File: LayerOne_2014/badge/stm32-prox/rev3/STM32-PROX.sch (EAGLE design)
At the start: 271 parts, among them IC1 IC_TPS6120XQFN10, IC10 74XX244, IC105 MCP1824T-250, IC106 MCP1824T-120, IC11 CD4066, IC13 PQ1X331M2ZP-3V3-LDO-SOT-23-5, IC14 AD8052, IC2 STM32F1_HIGH_DENSITY_LQFP64LQ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, IC3 PQ1X331M2ZP-3V3-LDO-SOT-23-5, IC4 HCU-INVERTER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

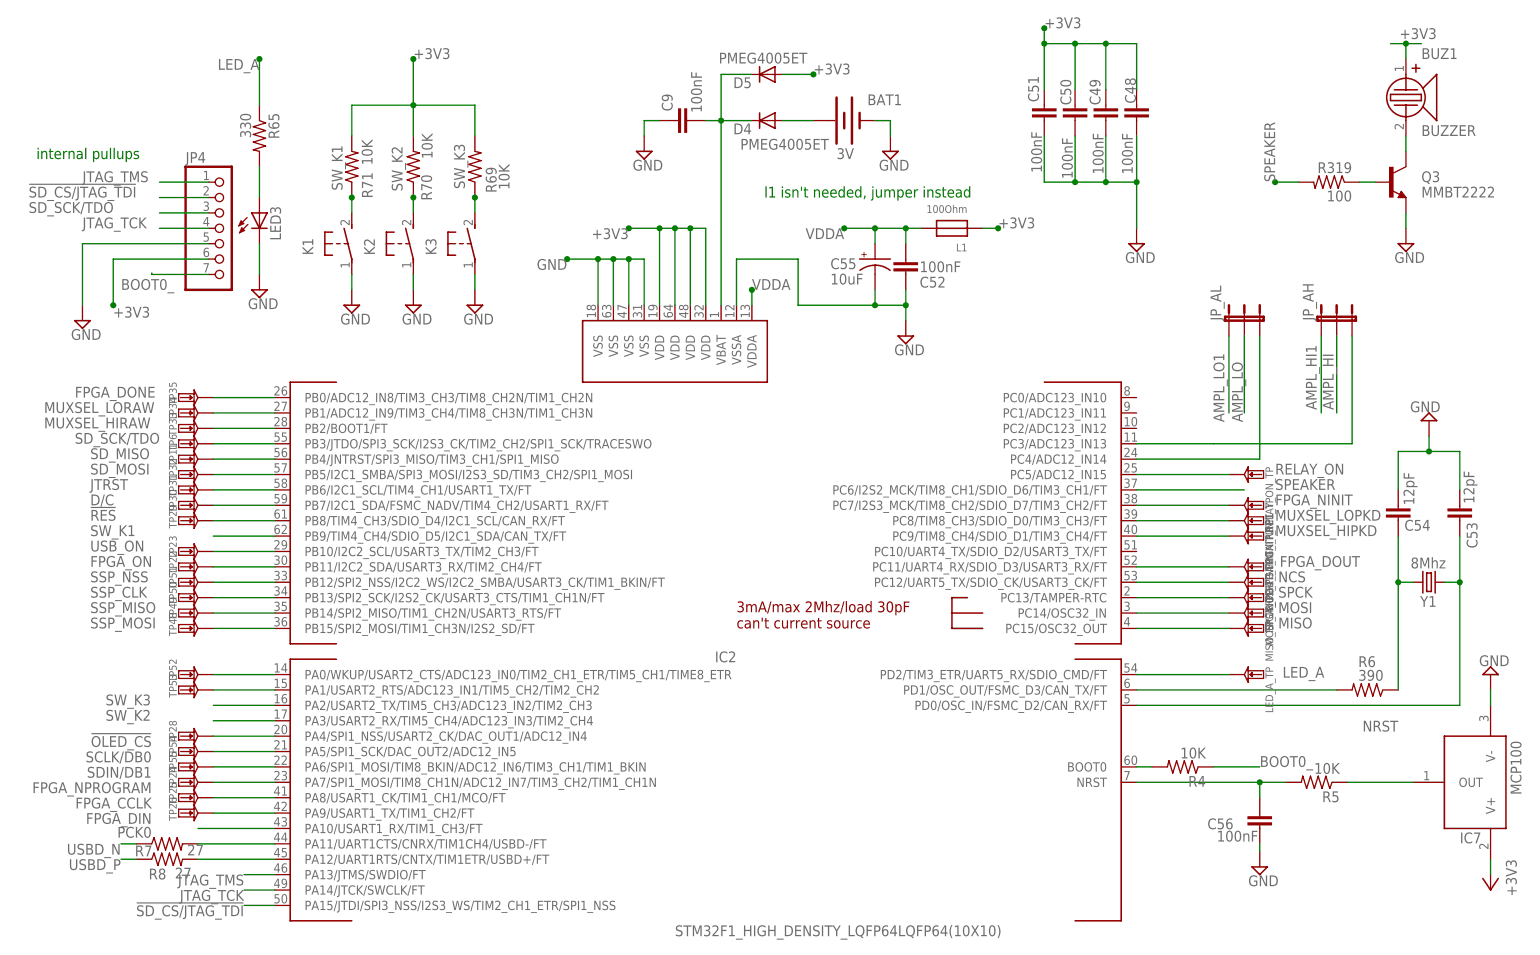
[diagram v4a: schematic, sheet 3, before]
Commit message: PB6 fixed on schematic for stm32f
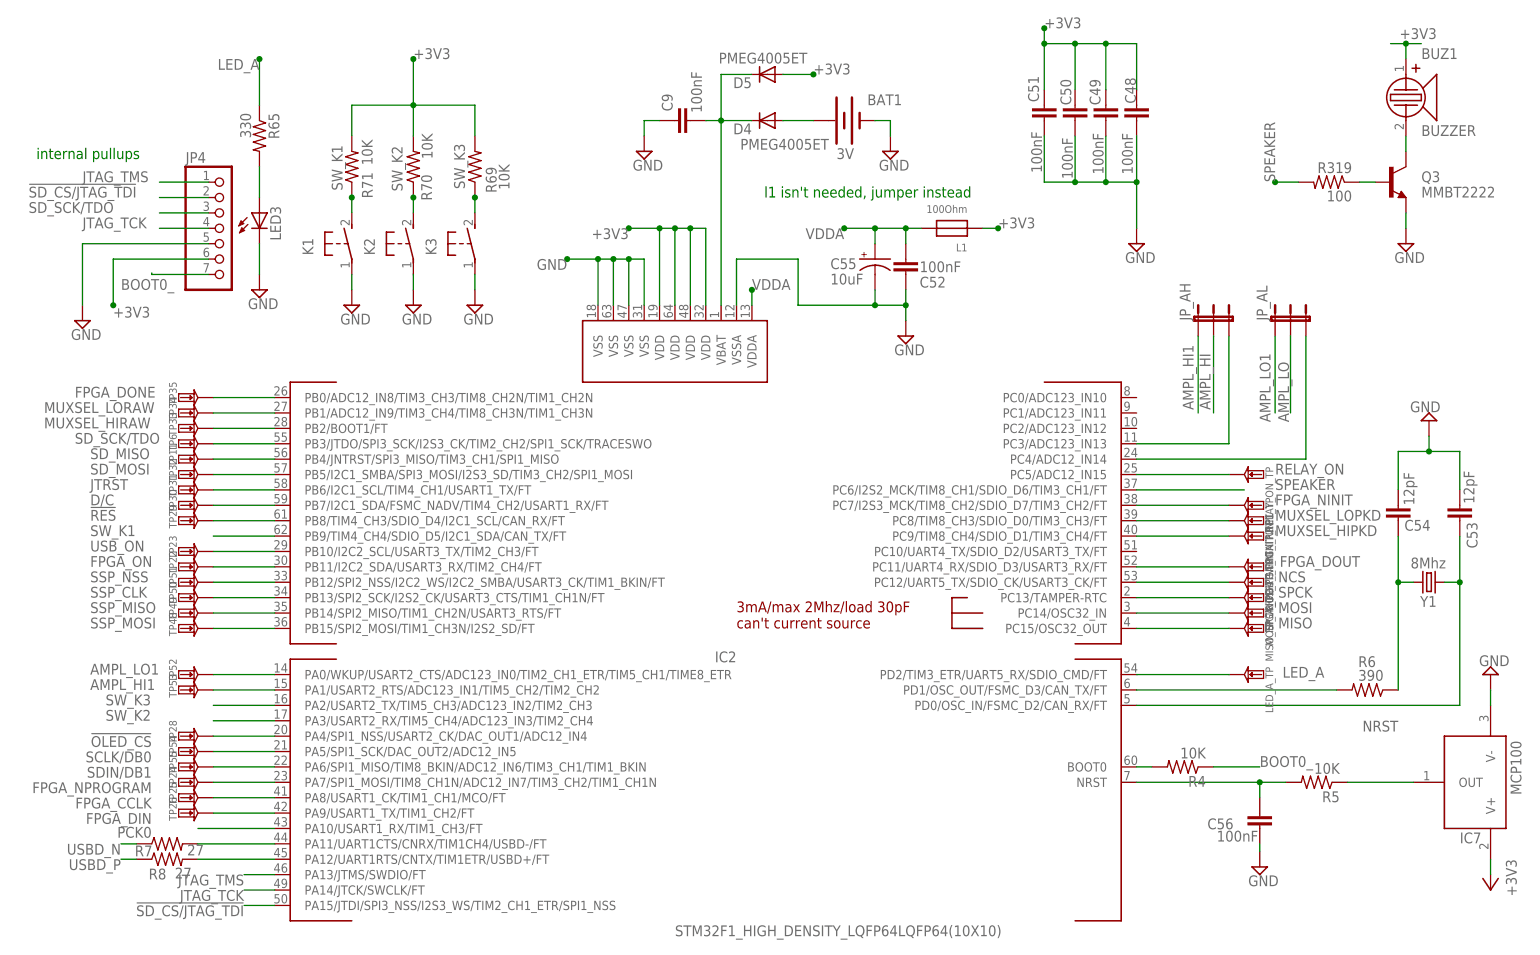
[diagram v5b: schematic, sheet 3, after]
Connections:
- new net N$29: U2G$1.L32P_1/GCLK4
- net SDIN/DB1: now also IC2.PA6/SPI1_MISO/TIM8_BKIN/ADC12_IN6/TIM3_CH1/TIM1_BKIN; no longer IC2.PA6/SPI1_MOSI/TIM8_BKIN/ADC12_IN6/TIM3_CH1/TIM1_BKIN
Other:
- moved on the sheet: JP_AH, JP_AL, OE4_TP
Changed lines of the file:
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@@
 <instance part="FPGA_NINIT_TP2" gate="G$1" x="220.98" y="48.26" rot="R270"/>
 <instance part="IC2" gate="G$1" x="127" y="27.94"/>
-<instance part="JP_AL" gate="G$1" x="218.44" y="83.82"/>
-<instance part="JP_AH" gate="G$1" x="233.68" y="83.82"/>
+<instance part="JP_AL" gate="G$1" x="226.06" y="83.82"/>
+<instance part="JP_AH" gate="G$1" x="213.36" y="83.82"/>
 </instances>
 <busses>
@@
 <pinref part="TP55" gate="G$1" pin="P$1"/>
 <wire x1="60.96" y1="10.16" x2="50.8" y2="10.16" width="0.1524" layer="91"/>
-<pinref part="IC2" gate="G$1" pin="PA6/SPI1_MOSI/TIM8_BKIN/ADC12_IN6/TIM3_CH1/TIM1_BKIN"/>
+<pinref part="IC2" gate="G$1" pin="PA6/SPI1_MISO/TIM8_BKIN/ADC12_IN6/TIM3_CH1/TIM1_BKIN"/>
 </segment>
 </net>
@@
 <segment>
 <pinref part="JP_AH" gate="G$1" pin="2"/>
-<wire x1="236.22" y1="81.28" x2="236.22" y2="68.58" width="0.1524" layer="91"/>
-<label x="235.712" y="69.088" size="1.778" layer="95" rot="R90"/>
+<wire x1="215.9" y1="81.28" x2="215.9" y2="68.58" width="0.1524" layer="91"/>
+<label x="215.392" y="69.088" size="1.778" layer="95" rot="R90"/>
 </segment>
 </net>
@@
 <segment>
 <pinref part="JP_AL" gate="G$1" pin="2"/>
-<wire x1="220.98" y1="81.28" x2="220.98" y2="68.58" width="0.1524" layer="91"/>
-<label x="220.726" y="67.056" size="1.778" layer="95" rot="R90"/>
+<wire x1="228.6" y1="81.28" x2="228.6" y2="68.58" width="0.1524" layer="91"/>
+<label x="228.346" y="67.056" size="1.778" layer="95" rot="R90"/>
 </segment>
 </net>
@@
 <segment>
 <pinref part="IC2" gate="G$1" pin="PC4/ADC12_IN14"/>
-<wire x1="203.2" y1="60.96" x2="223.52" y2="60.96" width="0.1524" layer="91"/>
+<wire x1="203.2" y1="60.96" x2="231.14" y2="60.96" width="0.1524" layer="91"/>
 <pinref part="JP_AL" gate="G$1" pin="3"/>
-<wire x1="223.52" y1="81.28" x2="223.52" y2="60.96" width="0.1524" layer="91"/>
+<wire x1="231.14" y1="81.28" x2="231.14" y2="60.96" width="0.1524" layer="91"/>
 </segment>
 </net>
@@
 <segment>
 <pinref part="IC2" gate="G$1" pin="PC3/ADC123_IN13"/>
-<wire x1="203.2" y1="63.5" x2="215.9" y2="63.5" width="0.1524" layer="91"/>
+<wire x1="203.2" y1="63.5" x2="218.44" y2="63.5" width="0.1524" layer="91"/>
 <pinref part="JP_AH" gate="G$1" pin="3"/>
-<wire x1="215.9" y1="63.5" x2="238.76" y2="63.5" width="0.1524" layer="91"/>
-<wire x1="238.76" y1="63.5" x2="238.76" y2="81.28" width="0.1524" layer="91"/>
+<wire x1="218.44" y1="63.5" x2="218.44" y2="81.28" width="0.1524" layer="91"/>
 </segment>
 </net>
@@
 <pinref part="TP52" gate="G$1" pin="P$1"/>
 <wire x1="60.96" y1="25.4" x2="50.8" y2="25.4" width="0.1524" layer="91"/>
+<label x="30.48" y="25.4" size="1.778" layer="95"/>
 </segment>
 <segment>
 <pinref part="JP_AL" gate="G$1" pin="1"/>
-<wire x1="218.44" y1="81.28" x2="218.44" y2="68.58" width="0.1524" layer="91"/>
-<label x="217.678" y="67.056" size="1.778" layer="95" rot="R90"/>
+<wire x1="226.06" y1="81.28" x2="226.06" y2="68.58" width="0.1524" layer="91"/>
+<label x="225.298" y="67.056" size="1.778" layer="95" rot="R90"/>
 </segment>
 </net>
@@
 <pinref part="TP53" gate="G$1" pin="P$1"/>
 <wire x1="60.96" y1="22.86" x2="50.8" y2="22.86" width="0.1524" layer="91"/>
+<label x="30.48" y="22.86" size="1.778" layer="95"/>
 </segment>
 <segment>
 <pinref part="JP_AH" gate="G$1" pin="1"/>
-<wire x1="233.68" y1="81.28" x2="233.68" y2="68.58" width="0.1524" layer="91"/>
-<label x="232.918" y="69.088" size="1.778" layer="95" rot="R90"/>
+<wire x1="213.36" y1="81.28" x2="213.36" y2="68.58" width="0.1524" layer="91"/>
+<label x="212.598" y="69.088" size="1.778" layer="95" rot="R90"/>
 </segment>
 </net>
@@
 <text x="-64.77" y="137.16" size="1.778" layer="91">do we need hswap</text>
 <text x="-12.7" y="152.4" size="1.778" layer="91">PCK0 is 24Mhz</text>
-<text x="-112.268" y="79.248" size="1.778" layer="91" rot="R90">SPI to ARM</text>
+<text x="-94.488" y="79.248" size="1.778" layer="91" rot="R90">SPI to ARM</text>
 </plain>
 <instances>
@@
 <attribute name="NAME" x="67.31" y="86.2965" size="1.27" layer="95"/>
 </instance>
-<instance part="OE4_TP" gate="G$1" x="76.2" y="91.44" smashed="yes" rot="R270">
-<attribute name="PARTNO" x="76.2" y="91.44" size="1.778" layer="96" rot="R270" display="off"/>
-<attribute name="OC_NEWARK" x="76.2" y="91.44" size="1.778" layer="96" rot="R270" display="off"/>
-<attribute name="MF" x="76.2" y="91.44" size="1.778" layer="96" rot="R270" display="off"/>
-<attribute name="MPN" x="76.2" y="91.44" size="1.778" layer="96" rot="R270" display="off"/>
-<attribute name="NAME" x="74.93" y="92.9005" size="1.27" layer="95"/>
+<instance part="OE4_TP" gate="G$1" x="68.58" y="91.44" smashed="yes" rot="R270">
+<attribute name="PARTNO" x="68.58" y="91.44" size="1.778" layer="96" rot="R270" display="off"/>
+<attribute name="OC_NEWARK" x="68.58" y="91.44" size="1.778" layer="96" rot="R270" display="off"/>
+<attribute name="MF" x="68.58" y="91.44" size="1.778" layer="96" rot="R270" display="off"/>
+<attribute name="MPN" x="68.58" y="91.44" size="1.778" layer="96" rot="R270" display="off"/>
+<attribute name="NAME" x="67.31" y="92.9005" size="1.27" layer="95"/>
 </instance>
 <instance part="ADC_NOE_TP" gate="G$1" x="7.62" y="-12.7" rot="R180">
@@
 <pinref part="U2" gate="G$1" pin="L32N_1/GCLK5"/>
 <wire x1="-5.08" y1="129.54" x2="-5.08" y2="144.78" width="0.1524" layer="91"/>
-<label x="-4.572" y="139.954" size="1.778" layer="95" rot="R270"/>
+<label x="-7.112" y="145.034" size="1.778" layer="95" rot="R270"/>
 <pinref part="PCK0_TP" gate="G$1" pin="P$1"/>
 </segment>
@@
 <segment>
 <pinref part="U2" gate="G$1" pin="L24P_6"/>
-<wire x1="-68.58" y1="63.5" x2="-92.456" y2="63.5" width="0.1524" layer="91"/>
-<label x="-98.298" y="62.484" size="1.778" layer="95"/>
+<wire x1="-68.58" y1="63.5" x2="-74.676" y2="63.5" width="0.1524" layer="91"/>
+<label x="-80.518" y="62.484" size="1.778" layer="95"/>
 </segment>
 </net>
@@
 <segment>
 <pinref part="U2" gate="G$1" pin="L40N_6"/>
-<wire x1="-68.58" y1="66.04" x2="-92.456" y2="66.04" width="0.1524" layer="91"/>
-<label x="-98.298" y="65.024" size="1.778" layer="95"/>
+<wire x1="-68.58" y1="66.04" x2="-74.676" y2="66.04" width="0.1524" layer="91"/>
+<label x="-80.518" y="65.024" size="1.778" layer="95"/>
 </segment>
 </net>
@@
 <segment>
 <pinref part="U2" gate="G$1" pin="L21N_2"/>
-<wire x1="43.18" y1="91.44" x2="73.66" y2="91.44" width="0.1524" layer="91"/>
-<label x="82.296" y="90.424" size="1.778" layer="95"/>
+<wire x1="43.18" y1="91.44" x2="66.04" y2="91.44" width="0.1524" layer="91"/>
+<label x="74.676" y="90.424" size="1.778" layer="95"/>
 <pinref part="OE4_TP" gate="G$1" pin="P$1"/>
 </segment>
@@
 <segment>
 <pinref part="U2" gate="G$1" pin="L23N_7"/>
-<wire x1="-68.58" y1="83.82" x2="-93.98" y2="83.82" width="0.1524" layer="91"/>
-<label x="-109.728" y="82.804" size="1.778" layer="95"/>
+<wire x1="-68.58" y1="83.82" x2="-76.2" y2="83.82" width="0.1524" layer="91"/>
+<label x="-91.948" y="82.804" size="1.778" layer="95"/>
 </segment>
 </net>
@@
 <segment>
 <pinref part="U2" gate="G$1" pin="L23P_7"/>
-<wire x1="-68.58" y1="86.36" x2="-93.98" y2="86.36" width="0.1524" layer="91"/>
-<label x="-109.728" y="85.344" size="1.778" layer="95"/>
+<wire x1="-68.58" y1="86.36" x2="-76.2" y2="86.36" width="0.1524" layer="91"/>
+<label x="-91.948" y="85.344" size="1.778" layer="95"/>
 </segment>
 </net>
@@
 <segment>
 <pinref part="U2" gate="G$1" pin="L21N_7"/>
-<wire x1="-68.58" y1="88.9" x2="-93.98" y2="88.9" width="0.1524" layer="91"/>
-<label x="-109.728" y="88.138" size="1.778" layer="95"/>
+<wire x1="-68.58" y1="88.9" x2="-76.2" y2="88.9" width="0.1524" layer="91"/>
+<label x="-91.948" y="88.138" size="1.778" layer="95"/>
 </segment>
 </net>
@@
 <segment>
 <pinref part="U2" gate="G$1" pin="L21P_7"/>
-<wire x1="-68.58" y1="91.44" x2="-93.98" y2="91.44" width="0.1524" layer="91"/>
-<label x="-109.728" y="90.424" size="1.778" layer="95"/>
+<wire x1="-68.58" y1="91.44" x2="-76.2" y2="91.44" width="0.1524" layer="91"/>
+<label x="-91.948" y="90.424" size="1.778" layer="95"/>
 </segment>
 </net>
@@
 <segment>
 <pinref part="U2" gate="G$1" pin="L01P_7/VRN_7"/>
-<wire x1="-68.58" y1="96.52" x2="-93.98" y2="96.52" width="0.1524" layer="91"/>
-<label x="-93.98" y="96.52" size="1.778" layer="95" rot="R180"/>
+<wire x1="-68.58" y1="96.52" x2="-76.2" y2="96.52" width="0.1524" layer="91"/>
+<label x="-76.2" y="96.52" size="1.778" layer="95" rot="R180"/>
 </segment>
 </net>
@@
 </segment>
 </net>
+<net name="N$29" class="0">
+<segment>
+<pinref part="U2" gate="G$1" pin="L32P_1/GCLK4"/>
+<wire x1="-2.54" y1="129.54" x2="-2.54" y2="134.62" width="0.1524" layer="91"/>
+</segment>
+</net>

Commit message: routing pass.
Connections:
- net AMPL_HI1: now also IC2.PA0/WKUP/USART2_CTS/ADC123_IN0/TIM2_CH1_ETR/TIM5_CH1/TIME8_ETR, TP52.P$1; no longer IC2.PA1/USART2_RTS/ADC123_IN1/TIM5_CH2/TIM2_CH2, TP53.P$1
- net AMPL_LO1: now also IC2.PA1/USART2_RTS/ADC123_IN1/TIM5_CH2/TIM2_CH2, TP53.P$1; no longer IC2.PA0/WKUP/USART2_CTS/ADC123_IN0/TIM2_CH1_ETR/TIM5_CH1/TIME8_ETR, TP52.P$1
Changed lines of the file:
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@@
 </class>
 <class number="2" name="power" width="0.2794" drill="0.254">
-<clearance class="2" value="0.3048"/>
 </class>
 </classes>
@@
 </segment>
 </net>
-<net name="+3V3" class="0">
+<net name="+3V3" class="2">
 <segment>
 <pinref part="Q2" gate="G$1" pin="C"/>
@@
 </busses>
 <nets>
-<net name="+3V3" class="0">
+<net name="+3V3" class="2">
 <segment>
 <wire x1="132.08" y1="86.36" x2="132.08" y2="99.06" width="0.1524" layer="91"/>
@@
 <net name="AMPL_LO1" class="0">
 <segment>
-<pinref part="IC2" gate="G$1" pin="PA0/WKUP/USART2_CTS/ADC123_IN0/TIM2_CH1_ETR/TIM5_CH1/TIME8_ETR"/>
-<pinref part="TP52" gate="G$1" pin="P$1"/>
-<wire x1="60.96" y1="25.4" x2="50.8" y2="25.4" width="0.1524" layer="91"/>
-<label x="30.48" y="25.4" size="1.778" layer="95"/>
-</segment>
-<segment>
 <pinref part="JP_AL" gate="G$1" pin="1"/>
 <wire x1="226.06" y1="81.28" x2="226.06" y2="68.58" width="0.1524" layer="91"/>
 <label x="225.298" y="67.056" size="1.778" layer="95" rot="R90"/>
 </segment>
-</net>
-<net name="AMPL_HI1" class="0">
 <segment>
 <pinref part="IC2" gate="G$1" pin="PA1/USART2_RTS/ADC123_IN1/TIM5_CH2/TIM2_CH2"/>
@@
 <label x="30.48" y="22.86" size="1.778" layer="95"/>
 </segment>
+</net>
+<net name="AMPL_HI1" class="0">
 <segment>
 <pinref part="JP_AH" gate="G$1" pin="1"/>
@@
 <label x="212.598" y="69.088" size="1.778" layer="95" rot="R90"/>
 </segment>
+<segment>
+<pinref part="TP52" gate="G$1" pin="P$1"/>
+<pinref part="IC2" gate="G$1" pin="PA0/WKUP/USART2_CTS/ADC123_IN0/TIM2_CH1_ETR/TIM5_CH1/TIME8_ETR"/>
+<wire x1="50.8" y1="25.4" x2="60.96" y2="25.4" width="0.1524" layer="91"/>
+<label x="30.48" y="25.4" size="1.778" layer="95"/>
+</segment>
 </net>
 </nets>
@@
 </segment>
 </net>
-<net name="+3V3" class="0">
+<net name="+3V3" class="2">
 <segment>
 <wire x1="142.24" y1="-29.21" x2="144.78" y2="-29.21" width="0.1524" layer="91"/>
@@
 </segment>
 </net>
-<net name="+3V3" class="0">
+<net name="+3V3" class="2">
 <segment>
 <pinref part="U3" gate="G$1" pin="VBAT"/>
@@
 </segment>
 </net>
-<net name="+3V3" class="0">
+<net name="+3V3" class="2">
 <segment>
 <pinref part="U4" gate="G$1" pin="VCC"/>
